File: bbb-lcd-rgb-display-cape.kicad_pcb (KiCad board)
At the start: 2 copper layers, 54.6 x 86.4 mm, 30 parts, among them P1 OrangePi-2G-IOT LCD Interface, P12 RS485, P8 BeagleBone_Black_Header, P9 BeagleBone_Black_Header, Sw1 DTSM-31N, Sw2 DTSM-31N, Sw3 DTSM-31N, Sw4 DTSM-31N, U5 TCN75A, U6 DS18B20U

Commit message: Continue schematic work
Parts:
- added C1: 100n/50V, Capacitors_Smd_0603:100nF_0603, F.Cu at (148.5, 97.8)
- added C2: 100n/50V, Capacitors_Smd_0603:100nF_0603, F.Cu at (146.0, 105.6)
- added C3: 100n/50V, Capacitors_Smd_0603:100nF_0603, F.Cu at (149.5, 104.8)
- added C4: 100n/50V, Capacitors_Smd_0603:100nF_0603, F.Cu at (145.1, 100.1)
- added C5: 1uF/6V3, Capacitors_Smd_0603:1uF_0603, F.Cu at (152.0, 100.1)
- added C6: 100nF/50V, Capacitors_Smd_0603:100nF_0603, F.Cu at (142.6, 106.2)
- added C7: 100nF/50V, Capacitors_Smd_0603:100nF_0603, F.Cu at (139.1, 106.2)
- added C8: 4.7uF/35V, Capacitors_Smd_0603:4_7uF_0603, F.Cu at (150.3, 102.5)
- added D1: NSR0530H-D, Diodes:NSR0530H-D_SOD323, F.Cu at (139.5, 103.5)
- added L1: 4u7H_CD32_SMD_Coil, Inductors:4u7H_SMD_CD32, F.Cu at (140.4, 99.3)
- added R1: 10k, Resistor_Smd_0603:10k_0603, F.Cu at (152.0, 97.8)
- added R2: 1k, Resistor_Smd_0603:1k_0603, F.Cu at (145.1, 97.8)
- added R3: 1k, Resistor_Smd_0603:1k_0603, F.Cu at (148.5, 100.1)
- added R4: 1k, Resistor_Smd_0603:1k_0603, F.Cu at (143.4, 103.2)
- added R5: 1k, Resistor_Smd_0603:1k_0603, F.Cu at (155.4, 97.8)
- added R6: 10R/1%/0.1Wat, Resistor_Smd_0603:10R_0603, F.Cu at (146.8, 102.5)
- added U1: 82357120100, ESD_Protectors:82357120100, F.Cu at (155.2, 99.9)
- added U2: 82357120100, ESD_Protectors:82357120100, F.Cu at (149.2, 106.9)
- added U3: 82357120100, ESD_Protectors:82357120100, F.Cu at (153.5, 102.2)
- added U4: 82357120100, ESD_Protectors:82357120100, F.Cu at (145.8, 107.7)
- added U7: TPS61169DCKR, Lcd_Backlight_Drivers:TPS61169DCKR, F.Cu at (138.2, 90.9)
- added U8: AP2127K-2.8TRG1, Linear:AP2127K-2.8TRG1_SOT23, F.Cu at (146.0, 92.2)
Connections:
- P1 pad 10: (no net) -> /B2
- P1 pad 11: (no net) -> /B3
- P1 pad 12: (no net) -> /B4
- P1 pad 13: (no net) -> /B5
- P1 pad 14: (no net) -> /G0
- P1 pad 15: (no net) -> /G1
- P1 pad 16: (no net) -> /G2
- P1 pad 17: (no net) -> /G3
- P1 pad 18: (no net) -> /G4
- P1 pad 19: (no net) -> /G5
- P1 pad 2: (no net) -> Net-(C3-Pad1)
- P1 pad 20: (no net) -> /R1
- P1 pad 21: (no net) -> /R1
- P1 pad 22: (no net) -> /R1
- P1 pad 23: (no net) -> /R1
- P1 pad 24: (no net) -> /R1
- P1 pad 26: (no net) -> /DE
- P1 pad 27: (no net) -> /PCLK
- P1 pad 28: (no net) -> /HSYNC
- P1 pad 29: (no net) -> /VSYNC
- P1 pad 3: (no net) -> GND
- P1 pad 31: (no net) -> GND
- P1 pad 32: (no net) -> 2V8
- P1 pad 33: (no net) -> GND
- P1 pad 35: (no net) -> GND
- P1 pad 36: (no net) -> 2V8
- P1 pad 37: (no net) -> Net-(P1-Pad37)
- P1 pad 38: (no net) -> Net-(P1-Pad38)
- P1 pad 39: (no net) -> Net-(P1-Pad39)
- P1 pad 4: (no net) -> 2V8
- P1 pad 40: (no net) -> Net-(P1-Pad40)
- P1 pad 8: (no net) -> GND
- P1 pad 9: (no net) -> /B1
- P8 pad 13: (no net) -> /BACKLIGHT_PWM
- P8 pad 15: (no net) -> /R1
- P8 pad 27: (no net) -> /VSYNC
- P8 pad 28: (no net) -> /PCLK
- P8 pad 29: (no net) -> /HSYNC
- P8 pad 30: (no net) -> /DE
- P8 pad 34: (no net) -> /G0
- P8 pad 36: (no net) -> /G1
- P8 pad 37: (no net) -> /G3
- P8 pad 38: (no net) -> /G2
- P8 pad 39: (no net) -> /G5
- P8 pad 40: (no net) -> /G4
- P8 pad 41: (no net) -> /B1
- P8 pad 43: (no net) -> /B3
- P8 pad 44: (no net) -> /B2
- P8 pad 45: (no net) -> /B5
- P8 pad 46: (no net) -> /B4

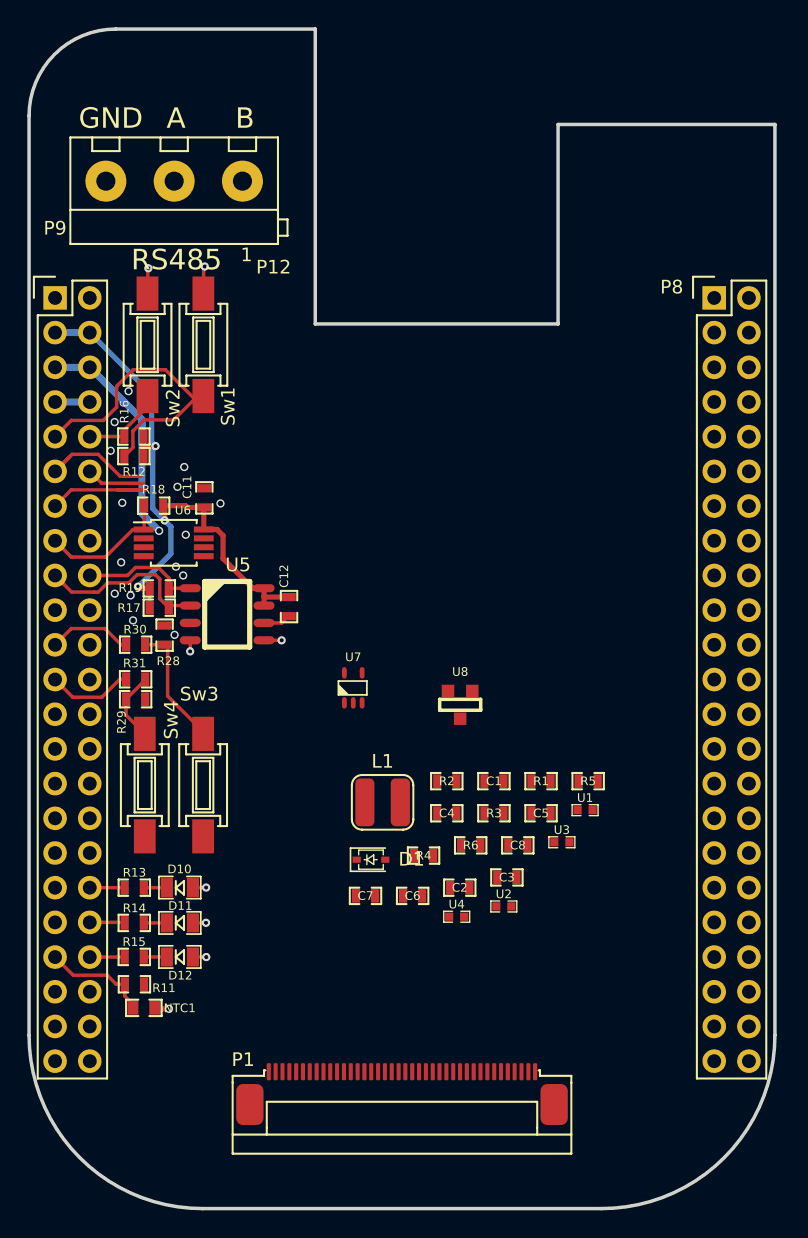
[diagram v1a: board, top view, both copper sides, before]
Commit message: Corrected schematic and added new elements
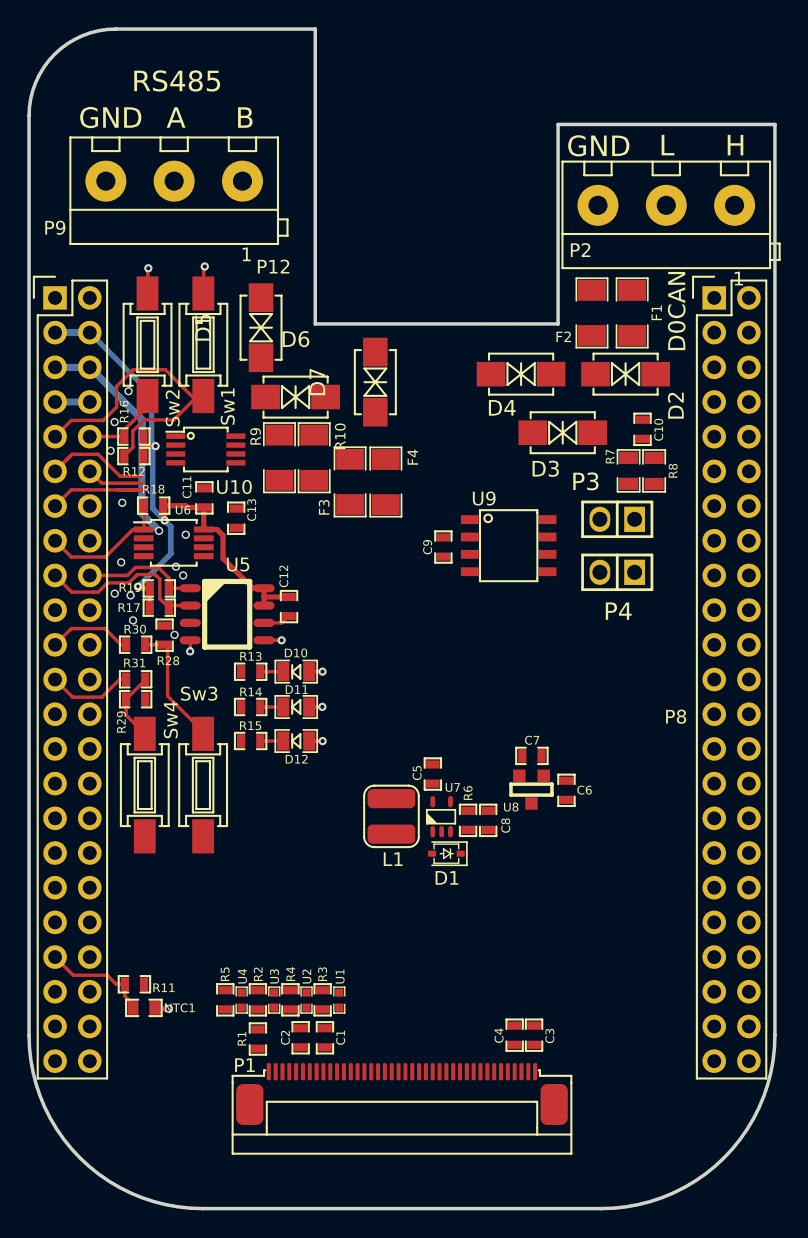
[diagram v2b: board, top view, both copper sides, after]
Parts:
- added C10: 100nF/50V, Capacitors_Smd_0603:100nF_0603, F.Cu at (159.4, 72.0)
- added C13: 100nF/50V, Capacitors_Smd_0603:100nF_0603, F.Cu at (129.6, 78.5)
- added C9: 100nF/50V, Capacitors_Smd_0603:100nF_0603, F.Cu at (144.8, 80.6)
- added D2: SMAJ18CA, Diodes:SMAJ18CA_SMD_DO214AC, F.Cu at (158.1, 68.0)
- added D3: SMAJ18CA, Diodes:SMAJ18CA_SMD_DO214AC, F.Cu at (153.5, 72.3)
- added D4: SMAJ18CA, Diodes:SMAJ18CA_SMD_DO214AC, F.Cu at (150.5, 68.0)
- added D5: SMAJ7.5CA, Diodes:SMAJ7.5CA_SMD_DO214AC, F.Cu at (131.5, 64.6)
- added D6: SMAJ18CA, Diodes:SMAJ18CA_SMD_DO214AC, F.Cu at (134.0, 69.6)
- added D7: SMAJ7.5CA, Diodes:SMAJ7.5CA_SMD_DO214AC, F.Cu at (139.8, 68.6)
- added F1: SN005-60, Smd_Ptc_Fuses:SN005-60, F.Cu at (158.6, 63.5)
- added F2: SN005-60, Smd_Ptc_Fuses:SN005-60, F.Cu at (155.7, 63.5)
- added F3: SN005-60, Smd_Ptc_Fuses:SN005-60, F.Cu at (138.0, 75.9)
- added F4: SN005-60, Smd_Ptc_Fuses:SN005-60, F.Cu at (140.6, 75.9)
- added P2: CAN BUS, Discrete_Connectors:DG301-5.0-03P-12-00A(H), F.Cu at (161.1, 55.6)
- added P3: TERM, Goldpin:Goldpin_2_2_54mm, F.Cu at (157.5, 78.6)
- added P4: TERM, Goldpin:Goldpin_2_2_54mm, F.Cu at (157.5, 82.5)
- added R10: CRCW120610R0FKEAHP, Resistor_Smd_1206:CRCW120610R0FKEAHP, F.Cu at (135.3, 74.1)
- added R7: 60.4R, Resistor_Smd_0805:60.4R_0805, F.Cu at (158.4, 75.0)
- added R8: 60.4R, Resistor_Smd_0805:60.4R_0805, F.Cu at (160.2, 75.1)
- added R9: CRCW120610R0FKEAHP, Resistor_Smd_1206:CRCW120610R0FKEAHP, F.Cu at (132.8, 74.1)
- added U10: ISL3172EIUZ, Communication_Interfaces:ISL3172EIUZ, F.Cu at (127.4, 73.5)
- added U9: IFX1050GVIOXUMA1, Communication_Interfaces:IFX1050GVIOXUMA1, F.Cu at (149.6, 80.5)
- moved REF** 44.5 mm to (140.8, 91.8)
- moved R5 31.0 mm to (128.8, 113.8), turned to 90 degrees
- moved R1 28.0 mm to (131.2, 116.6), turned to 90 degrees
- moved U3 24.0 mm to (132.4, 113.8), turned to -90 degrees
- moved U1 22.7 mm to (137.2, 113.8), turned to -90 degrees
- moved C1 22.5 mm to (136.1, 116.6), turned to 90 degrees
- moved R2 21.2 mm to (131.2, 113.8), turned to 90 degrees
- moved R3 18.5 mm to (136.0, 113.8), turned to -90 degrees
- moved D10 18.0 mm to (134.0, 89.7)
- moved D12 18.0 mm to (134.0, 94.8)
- moved R13 18.0 mm to (130.7, 89.8)
- moved R15 18.0 mm to (130.7, 94.8)
- moved D11 18.0 mm to (134.0, 92.3)
- moved R14 18.0 mm to (130.7, 92.3)
- moved C4 17.0 mm to (150.0, 116.4), turned to 90 degrees
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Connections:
- net Net-(P9-Pad15) renamed /GPIO1_16
- C3 pad 1: Net-(C3-Pad1) -> /LCD Display/BACKLIGHT_LOW
- C5 pad 1: /LCD Display/POWER_SUPPLY_2.7-5.5V -> 5V
- C6 pad 1: /LCD Display/POWER_SUPPLY_2.7-5.5V -> 5V
- L1 pad 1: /LCD Display/POWER_SUPPLY_2.7-5.5V -> 5V
- P1 pad 1: (no net) -> /LCD Display/BACKLIGHT_HIGH
- P1 pad 2: Net-(C3-Pad1) -> /LCD Display/BACKLIGHT_LOW
- P1 pad 25: (no net) -> /GPIO0_2
- P1 pad 30: (no net) -> /GPIO3_19
- P1 pad 33: GND -> /LCD Display/BACKLIGHT_LOW
- P1 pad 34: (no net) -> /LCD Display/BACKLIGHT_HIGH
- P1 pad 5: (no net) -> /SPI1_CS1
- P1 pad 6: (no net) -> /SPI1_SCK
- P1 pad 7: (no net) -> /SPI1_MOSI
- P12 pad 1: (no net) -> /RS485/RS485_A
- P12 pad 2: (no net) -> /RS485/RS485_B
- P9 pad 11: (no net) -> /UART4_RX
- P9 pad 12: (no net) -> /GPIO1_28
- P9 pad 13: (no net) -> /UART4_TX
- P9 pad 14: (no net) -> /GPIO1_18
- P9 pad 19: (no net) -> /DCAN0_RX
- P9 pad 20: (no net) -> /DCAN0_TX
- P9 pad 21: /GPIO1_17 -> (no net)
- P9 pad 22: (no net) -> /GPIO0_2
- P9 pad 23: /GPIO3_21 -> /GPIO1_17
- P9 pad 24: (no net) -> /GPIO0_15
- P9 pad 26: (no net) -> /GPIO0_14
- P9 pad 27: (no net) -> /GPIO3_19
- P9 pad 30: (no net) -> /SPI1_MOSI
- P9 pad 31: (no net) -> /SPI1_SCK
- P9 pad 35: (no net) -> Net-(P9-Pad35)
- P9 pad 36: /AIN5 -> (no net)
- P9 pad 37: (no net) -> Net-(P9-Pad37)
- P9 pad 38: /AIN3 -> (no net)
- P9 pad 40: /AIN1 -> (no net)
- P9 pad 41: (no net) -> /GPIO0_20
- P9 pad 42: (no net) -> /SPI1_CS1
- R1 pad 2: /LCD Display/TP_IRQ -> /GPIO0_20
- R13 pad 1: /AIN5 -> /GPIO1_17
- R14 pad 1: /AIN3 -> /GPIO0_15
- R15 pad 1: /AIN1 -> /GPIO0_14
- R2 pad 1: /LCD Display/TP_IRQ -> /GPIO0_20
- R3 pad 1: (no net) -> /I2C1_SDA
- R30 pad 2: /GPIO1_17 -> Net-(P9-Pad35)
- R31 pad 2: /GPIO3_21 -> Net-(P9-Pad37)
- R4 pad 1: (no net) -> /I2C1_SCL
- R5 pad 1: (no net) -> /GPIO1_18
- U7 pad 5: /LCD Display/POWER_SUPPLY_2.7-5.5V -> 5V
- U8 pad 3: /LCD Display/POWER_SUPPLY_2.7-5.5V -> 5V
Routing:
- net Net-(P9-Pad37): track 0.00 -> 6.28 mm
- net /GPIO3_21: track 6.28 -> 0.00 mm
- net Net-(P9-Pad35): track 0.00 -> 6.18 mm
- net /GPIO1_17: track 6.18 -> 0.00 mm
- net /AIN3: track 2.58 -> 0.00 mm
- net /AIN1: track 2.56 -> 0.00 mm
- net /AIN5: track 2.56 -> 0.00 mm
- net GND: vias 22 -> 19
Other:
- board text added: "D0CAN"
- board text added: "H"
- board text added: "L"

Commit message: RC1
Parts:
- moved C2 0.24 mm to (134.5, 116.8)
- turned P4 to 0 degrees
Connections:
- P1 pad 21: /R1 -> /R2
- P1 pad 22: /R1 -> /R3
- P1 pad 23: /R1 -> /R4
- P1 pad 24: /R1 -> /R5
- P8 pad 31: (no net) -> /R3
- P8 pad 32: (no net) -> /R2
- P8 pad 33: (no net) -> /R4
- P8 pad 35: (no net) -> /R5
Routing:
- net 5V: track 18.4 -> 96.9 mm, vias 1 -> 3
- net 2V8: track 0.00 -> 64.4 mm, vias 0 -> 6
- net 3V3: track 46.7 -> 108.4 mm, vias 4 -> 7
- net /GPIO1_18: track 0.00 -> 50.0 mm, vias 0 -> 2
- net /LCD Display/BACKLIGHT_HIGH: track 0.00 -> 49.9 mm, vias 0 -> 2
- net /R1: track 0.00 -> 48.9 mm, vias 0 -> 1
- net /LCD Display/BACKLIGHT_LOW: track 0.00 -> 48.4 mm, vias 0 -> 2
- net /SPI1_SCK: track 0.00 -> 46.5 mm, vias 0 -> 1
- net /GPIO0_2: track 0.00 -> 44.1 mm, vias 0 -> 1
- net /SPI1_MOSI: track 0.00 -> 43.0 mm, vias 0 -> 1
- net /PCLK: track 0.00 -> 41.1 mm, vias 0 -> 1
- net /VSYNC: track 0.00 -> 39.7 mm, vias 0 -> 1
- net /SPI1_CS1: track 0.00 -> 38.7 mm
- net /DE: track 0.00 -> 38.6 mm, vias 0 -> 1
- net /GPIO3_19: track 0.00 -> 38.1 mm, vias 0 -> 2
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
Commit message: Finalized project
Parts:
- removed D4, D6: SMAJ18CA, Diodes:SMAJ18CA_SMD_DO214AC
- removed D5, D7: SMAJ7.5CA, Diodes:SMAJ7.5CA_SMD_DO214AC
- added R20: 0R, Resistor_Smd_0603:0R_0603, F.Cu at (151.4, 101.1)
- added R21: 0R, Resistor_Smd_0603:0R_0603, F.Cu at (153.7, 98.5)
- added R22: 0R, Resistor_Smd_0603:0R_0603, F.Cu at (154.4, 110.2)
- D2: value SMAJ18CA -> PESD2CAN; footprint Diodes:SMAJ18CA_SMD_DO214AC -> ESD_Protectors:PESD2CAN.215
- D3: value SMAJ18CA -> SM712.TCT; footprint Diodes:SMAJ18CA_SMD_DO214AC -> ESD_Protectors:SM712.TCT
- moved D3 19.7 mm to (134.1, 69.0), turned to 0 degrees
- moved C6 3.24 mm to (153.6, 95.2)
- moved D2 1.80 mm to (156.6, 68.9)
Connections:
- D2 pad 1: GND -> Net-(U9-Pad6)
- D2 pad 2: Net-(D2-Pad2) -> Net-(P3-Pad2)
- D3 pad 1: Net-(D2-Pad2) -> Net-(R10-Pad1)
- D3 pad 2: Net-(D3-Pad2) -> Net-(R9-Pad1)
- F1 pad 1: Net-(D2-Pad2) -> Net-(P3-Pad2)
- F2 pad 1: Net-(D3-Pad2) -> Net-(U9-Pad6)
- F3 pad 1: Net-(D5-Pad2) -> Net-(R9-Pad1)
- F4 pad 1: Net-(D6-Pad2) -> Net-(R10-Pad1)
- P1 pad 1: /LCD Display/BACKLIGHT_HIGH -> /LCD Display/BACKLIGHT_VDD
- P1 pad 34: /LCD Display/BACKLIGHT_HIGH -> Net-(P1-Pad34)
- P3 pad 2: Net-(D2-Pad2) -> Net-(P3-Pad2)
- P4 pad 1: Net-(D3-Pad2) -> Net-(U9-Pad6)
- R10 pad 1: Net-(D6-Pad2) -> Net-(R10-Pad1)
- R9 pad 1: Net-(D5-Pad2) -> Net-(R9-Pad1)
- U9 pad 6: Net-(D3-Pad2) -> Net-(U9-Pad6)
- U9 pad 7: Net-(D2-Pad2) -> Net-(P3-Pad2)
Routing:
- net /LCD Display/BACKLIGHT_HIGH: track 49.9 -> 5.94 mm, vias 2 -> 0
- net Net-(P1-Pad34): track 0.00 -> 36.9 mm, vias 0 -> 2
- net Net-(U9-Pad6): track 0.00 -> 23.7 mm
- net Net-(D3-Pad2): track 22.9 -> 0.00 mm
- net /LCD Display/BACKLIGHT_VDD: track 0.00 -> 22.9 mm
- net Net-(D2-Pad2): track 19.2 -> 0.00 mm
- net Net-(P3-Pad2): track 0.00 -> 18.8 mm
- net Net-(D5-Pad2): track 17.8 -> 0.00 mm
- net Net-(R10-Pad1): track 0.00 -> 12.7 mm
- net Net-(D6-Pad2): track 11.0 -> 0.00 mm
- net Net-(R9-Pad1): track 0.00 -> 10.9 mm
- net 5V: track 96.9 -> 99.3 mm
- net GND: track 47.5 -> 48.7 mm, vias 49 -> 56

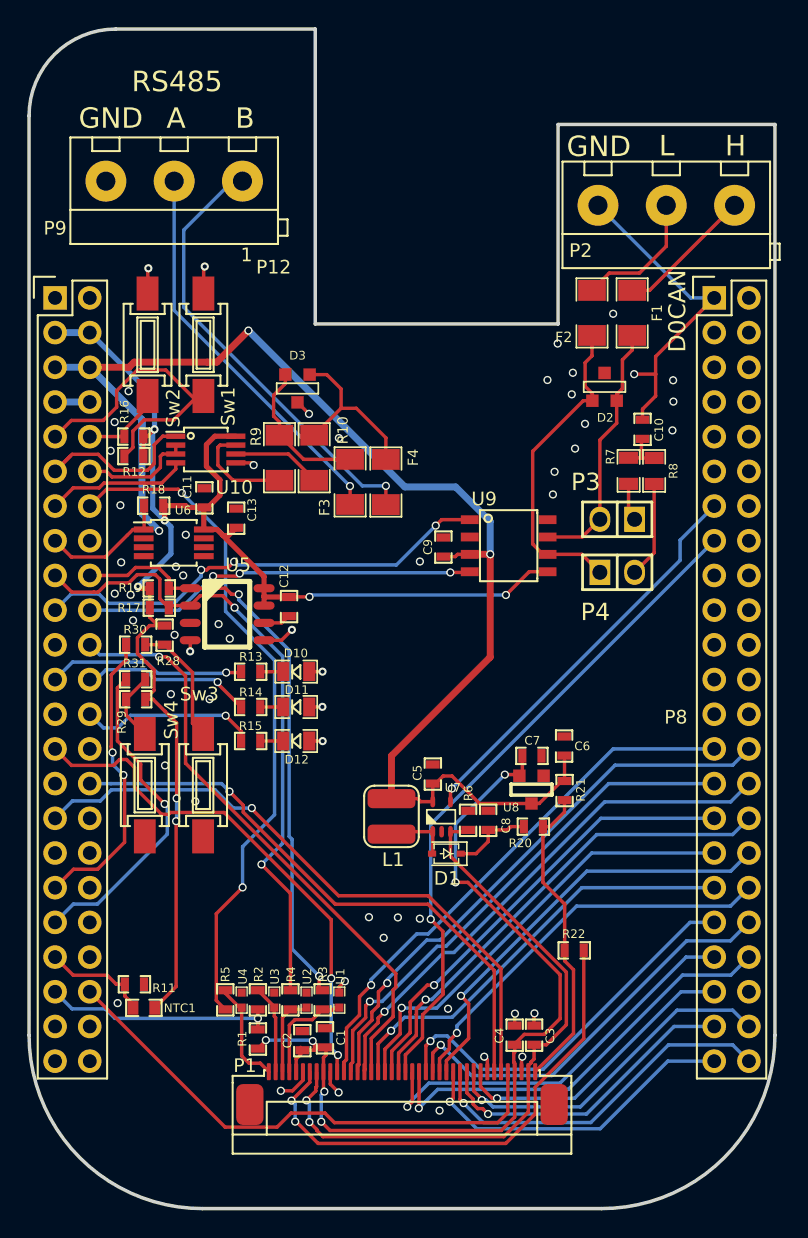
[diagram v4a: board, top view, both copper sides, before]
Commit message: Updated display pwm backlight section, regenerated gerbers again
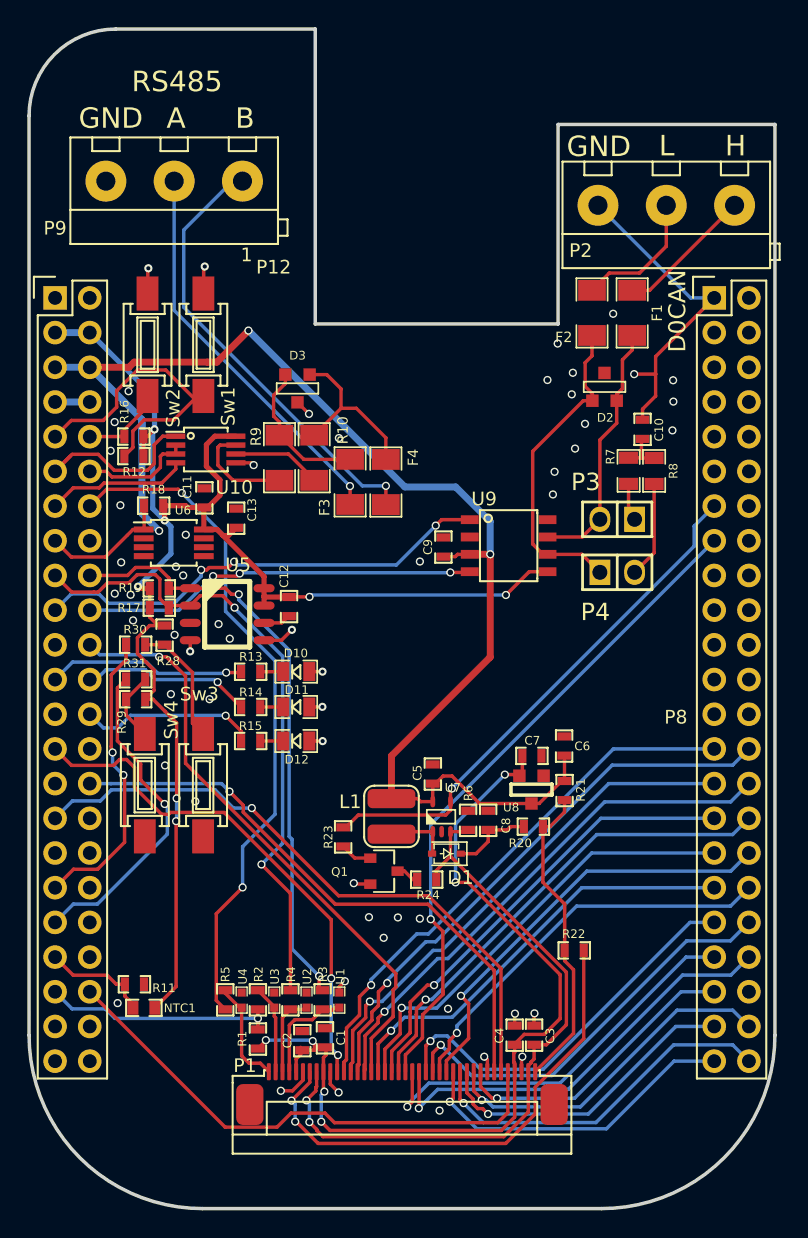
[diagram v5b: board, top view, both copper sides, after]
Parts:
- added Q1: BC847B, Transistor_Bipolar:BC847B_SOT23, F.Cu at (140.5, 104.4)
- added R23: 10k, Resistor_Smd_0603:10k_0603, F.Cu at (137.5, 101.8)
- added R24: 10R/1%/0.1Wat, Resistor_Smd_0603:10R_0603, F.Cu at (143.6, 105.0)
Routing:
- net /BACKLIGHT_PWM: track 29.6 -> 38.7 mm
- net Net-(R23-Pad2): track 0.00 -> 2.20 mm
- net /LCD Display/BACKLIGHT_LOW: track 48.4 -> 50.6 mm
- net Net-(R24-Pad2): track 0.00 -> 1.69 mm
- net GND: track 48.7 -> 49.8 mm, vias 56 -> 57
